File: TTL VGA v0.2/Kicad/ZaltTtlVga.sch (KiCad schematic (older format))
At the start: 2 parts

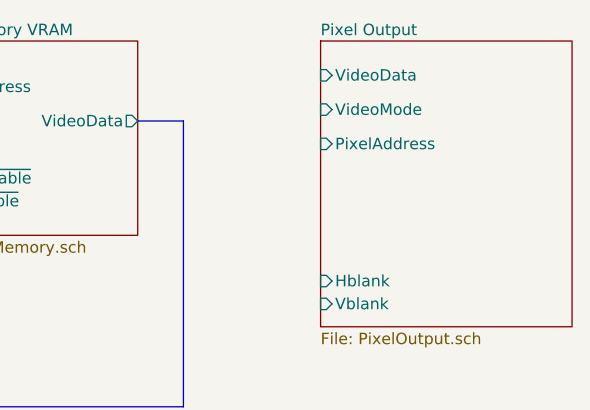
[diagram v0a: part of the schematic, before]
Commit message: video bit mux
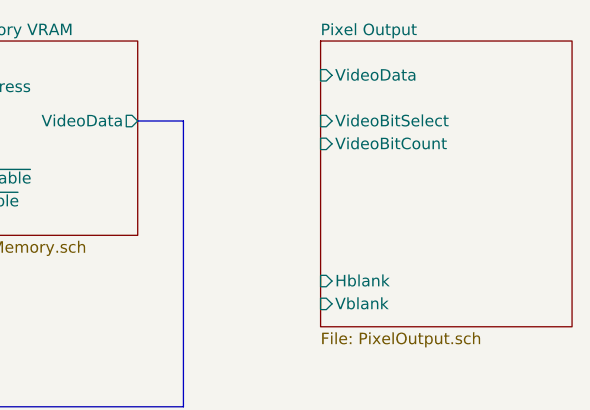
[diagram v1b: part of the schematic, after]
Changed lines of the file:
@@
 F3 "Vblank" I L 8050 1950 50
 F4 "VideoData" I L 8050 950 50
-F5 "VideoMode" I L 8050 1100 50
-F6 "PixelAddress" I L 8050 1250 50
+F5 "VideoBitSelect" I L 8050 1150 50
+F6 "VideoBitCount" I L 8050 1250 50
 $EndSheet
 $Comp

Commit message: update kicad
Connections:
- net labels added: A0, A1, A2, Hblank, PA0, PA1, PA2, Vblank, ~CDS0, ~CDS1, ~CDS2, ~VM1, ~VM2, ~VM3
- wire segments 61 -> 83

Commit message: Update
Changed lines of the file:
@@
 Wire Wire Line
 	8750 1950 8400 1950
+Text Label 8450 1850 0    50   ~ 0
+Hblank
+Text Label 8450 1950 0    50   ~ 0
+Vblank
+Text Label 2000 1400 0    50   ~ 0
+Hblank
+Text Label 2000 1500 0    50   ~ 0
+Vblank
+Wire Bus Line
+	3300 2350 2550 2350
+Wire Bus Line
+	2550 2350 2550 4100
+Wire Bus Line
+	2550 4100 4000 4100
+Wire Bus Line
+	4000 4100 4000 4700
 Wire Bus Line
 	7200 2500 7200 2700
@@
 Wire Bus Line
 	1150 4700 1150 6100
-Text Label 8450 1850 0    50   ~ 0
-Hblank
-Text Label 8450 1950 0    50   ~ 0
-Vblank
-Text Label 2000 1400 0    50   ~ 0
-Hblank
-Text Label 2000 1500 0    50   ~ 0
-Vblank
+Connection ~ 4000 4700
 $EndSCHEMATC
